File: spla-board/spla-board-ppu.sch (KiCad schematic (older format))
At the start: 20 parts, among them J15 J_DPULL, J5 J_PPURESET, U10 SNES_PPU1, U11 SNES_PPU2, U12 VRAM, U13 VRAM

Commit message: schematic: Add Digikey and ManufacturerId fields to big components.
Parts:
- U10, U11, U12, U13: Digikey (none) -> N/A; Manufacturer Id (none) -> N/A
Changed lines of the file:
@@
 F 2 "SPLA:QFP-100_14x20mm_P0.635mm" H 5700 8300 50  0001 C CNN
 F 3 "" H 5700 8300 50  0001 C CNN
+F 4 "N/A" H 5650 6100 50  0001 C CNN "Digikey"
+F 5 "N/A" H 5650 6100 50  0001 C CNN "Manufacturer Id"
 	1    5650 6100
 	1    0    0    -1
@@
 F 2 "SPLA:SOP-28_17x8mm_P1.27mm" H 9050 4050 50  0001 C CNN
 F 3 "" H 9050 4050 50  0001 C CNN
+F 4 "N/A" H 9050 4050 50  0001 C CNN "Digikey"
+F 5 "N/A" H 9050 4050 50  0001 C CNN "Manufacturer Id"
 	1    9050 4050
 	1    0    0    -1
@@
 F 2 "SPLA:SOP-28_17x8mm_P1.27mm" H 9050 6350 50  0001 C CNN
 F 3 "" H 9050 6350 50  0001 C CNN
+F 4 "N/A" H 9050 6350 50  0001 C CNN "Digikey"
+F 5 "N/A" H 9050 6350 50  0001 C CNN "Manufacturer Id"
 	1    9050 6350
 	1    0    0    -1
@@
 F 2 "SPLA:QFP-100_14x20mm_P0.635mm" H 12250 8300 50  0001 C CNN
 F 3 "" H 12250 8300 50  0001 C CNN
+F 4 "N/A" H 12200 6100 50  0001 C CNN "Digikey"
+F 5 "N/A" H 12200 6100 50  0001 C CNN "Manufacturer Id"
 	1    12200 6100
 	1    0    0    -1

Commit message: schematic: Add part numbers for pinheaders (albeit that these are breakaways, and it's not one-per-part).
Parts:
- J15, J5: Digikey (none) -> S1011EC-40-ND; Manufacturer Id (none) -> PRPC040SAAN-RC
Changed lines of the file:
@@
 F 2 "Connector_PinHeader_2.54mm:PinHeader_1x03_P2.54mm_Vertical" H 3250 9600 50  0001 C CNN
 F 3 "~" H 3250 9600 50  0001 C CNN
+F 4 "S1011EC-40-ND" H 3250 9600 50  0001 C CNN "Digikey"
+F 5 "PRPC040SAAN-RC" H 3250 9600 50  0001 C CNN "Manufacturer Id"
 	1    3250 9600
 	-1   0    0    1
@@
 F 2 "Connector_PinHeader_2.54mm:PinHeader_1x03_P2.54mm_Vertical" H 8050 1900 50  0001 C CNN
 F 3 "~" H 8050 1900 50  0001 C CNN
+F 4 "S1011EC-40-ND" H 8050 1900 50  0001 C CNN "Digikey"
+F 5 "PRPC040SAAN-RC" H 8050 1900 50  0001 C CNN "Manufacturer Id"
 	1    8050 1900
 	0    -1   -1   0

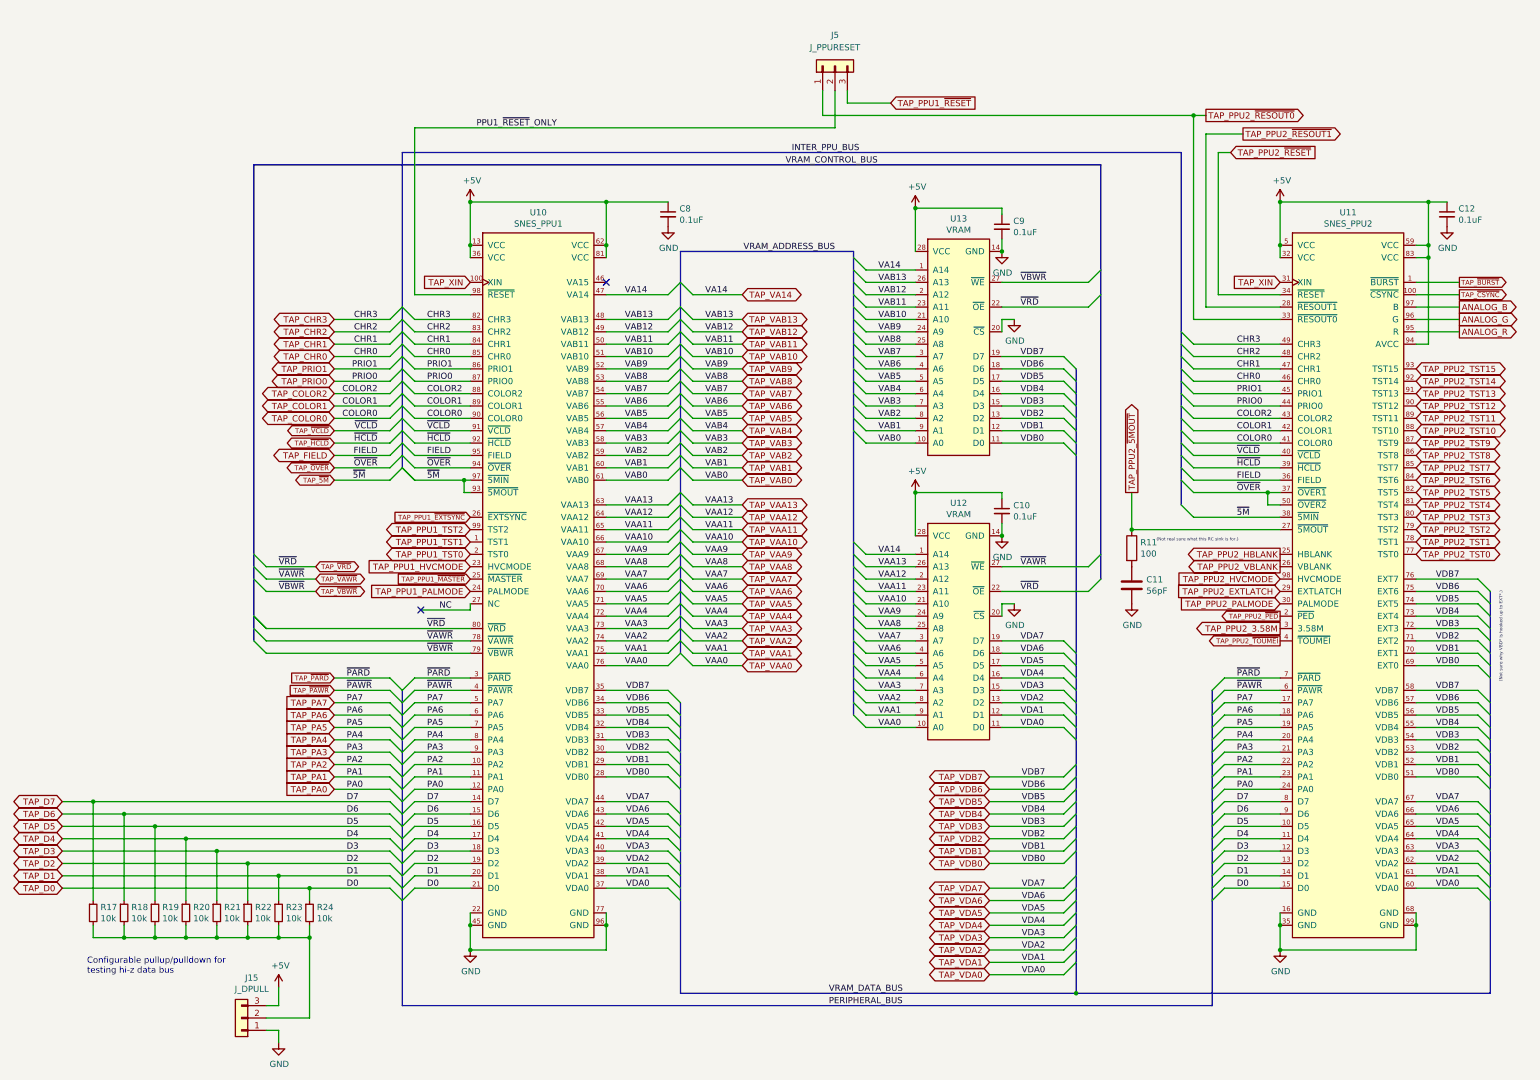
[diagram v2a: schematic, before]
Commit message: schematic/pcb: Add BoM-only symbols.
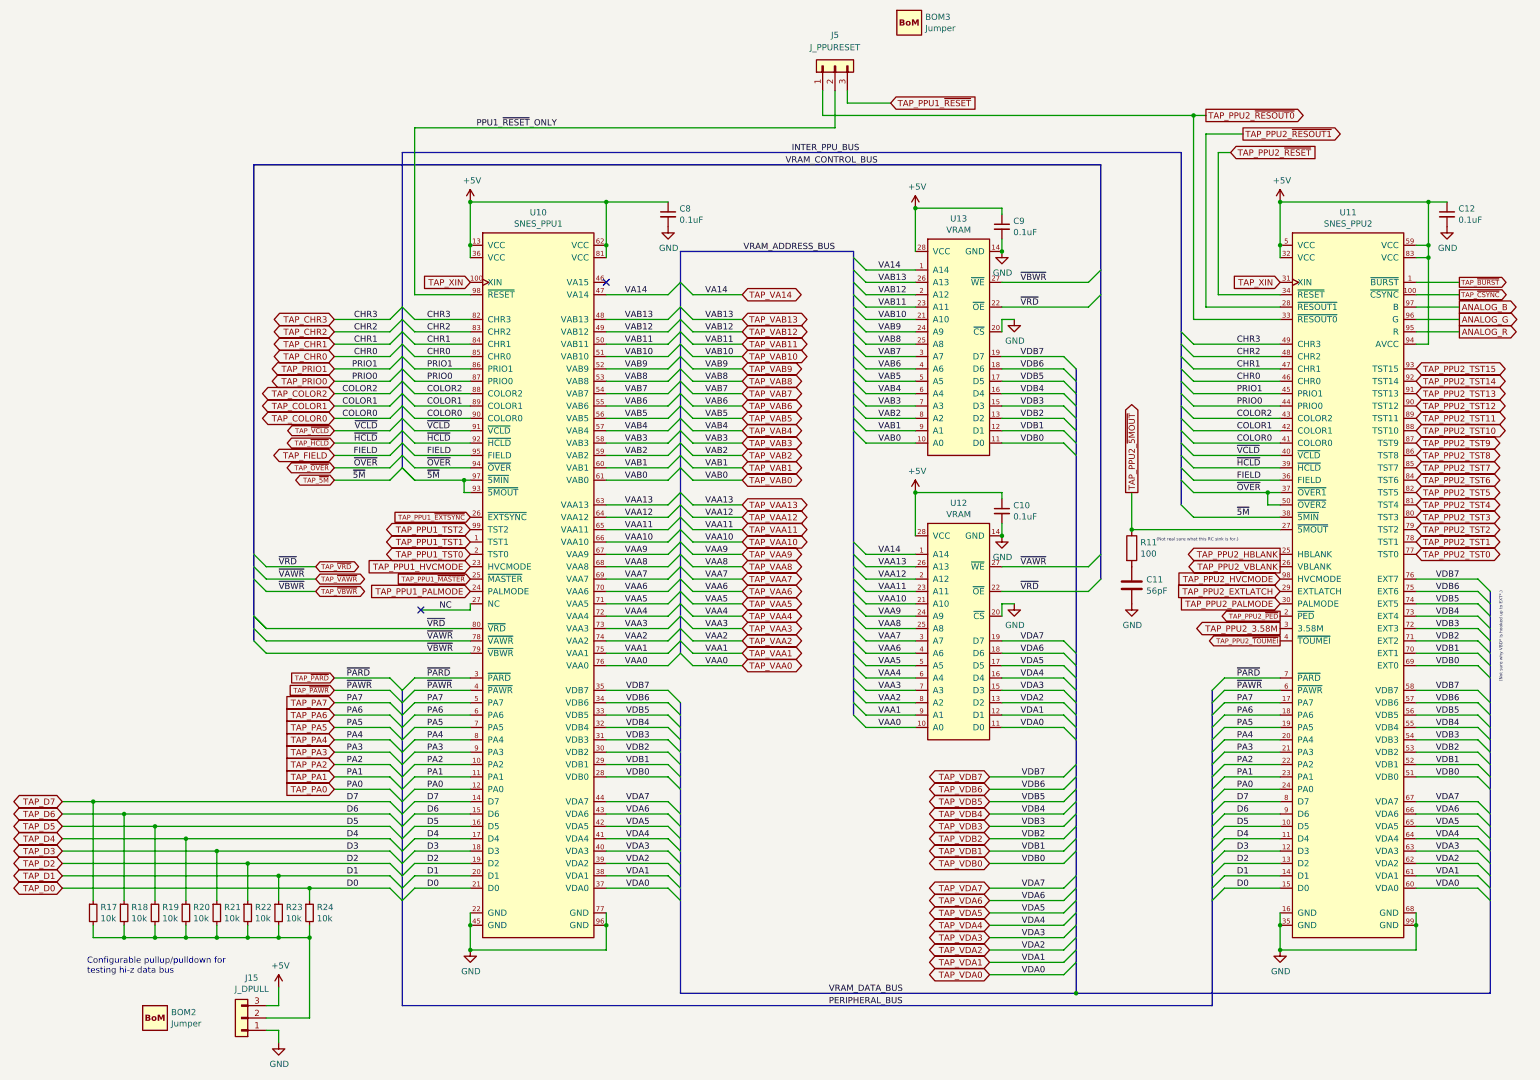
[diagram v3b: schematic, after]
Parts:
- added BOM2, BOM3: Jumper, SPLA:BoM, symbol SPLA:BomExtra
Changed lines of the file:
@@
 Wire Wire Line
 	4650 2400 8050 2400
+$Comp
+L SPLA:BomExtra BOM3
+U 1 1 5EAB9445
+P 8650 1550
+F 0 "BOM3" H 8780 1596 50  0000 L CNN
+F 1 "Jumper" H 8780 1505 50  0000 L CNN
+F 2 "SPLA:BoM" H 8650 1550 50  0001 C CNN
+F 3 "" H 8650 1550 50  0001 C CNN
+F 4 "S9337-ND" H 8650 1550 50  0001 C CNN "Digikey"
+F 5 "QPC02SXGN-RC" H 8650 1550 50  0001 C CNN "Manufacturer Id"
+	1    8650 1550
+	1    0    0    -1
+$EndComp
+$Comp
+L SPLA:BomExtra BOM2
+U 1 1 5EAB9764
+P 2550 9600
+F 0 "BOM2" H 2680 9646 50  0000 L CNN
+F 1 "Jumper" H 2680 9555 50  0000 L CNN
+F 2 "SPLA:BoM" H 2550 9600 50  0001 C CNN
+F 3 "" H 2550 9600 50  0001 C CNN
+F 4 "S9337-ND" H 2550 9600 50  0001 C CNN "Digikey"
+F 5 "QPC02SXGN-RC" H 2550 9600 50  0001 C CNN "Manufacturer Id"
+	1    2550 9600
+	1    0    0    -1
+$EndComp
 Wire Bus Line
 	10200 2700 10200 6050

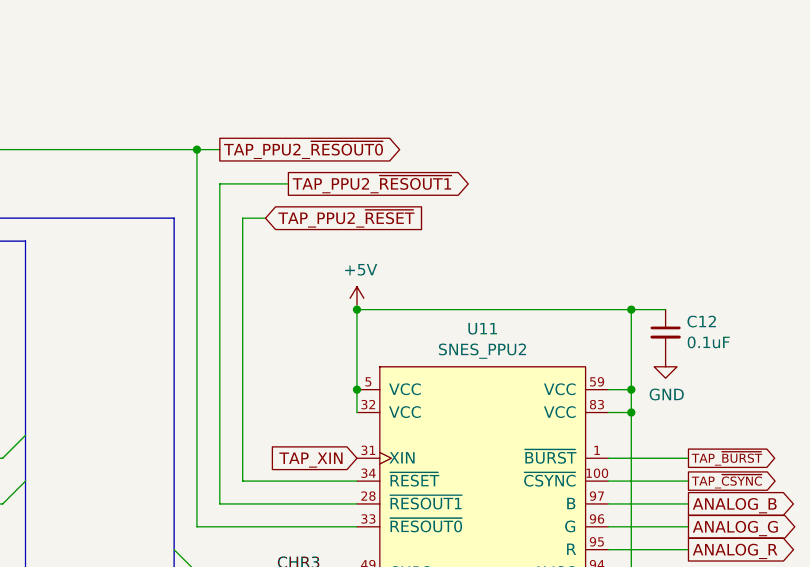
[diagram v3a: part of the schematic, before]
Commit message: schematic/pcb: Add pullup to SPI_CS and pulldown to PPU2_RESET.
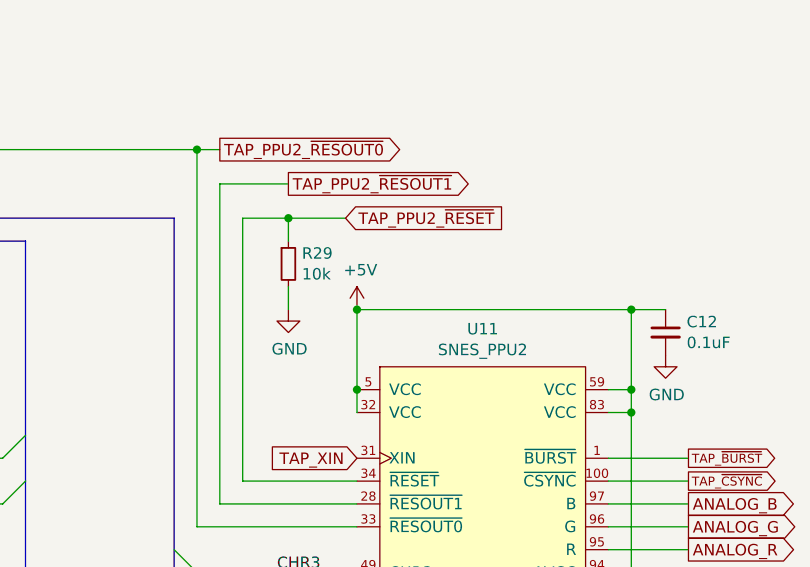
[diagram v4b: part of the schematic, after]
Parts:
- added R29: 10k, Resistor_SMD:R_0603_1608Metric, symbol Device:R_Small
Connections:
- net GND: now also R29.2
- net TAP_PPU2_~RESET~: now also R29.1
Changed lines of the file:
@@
 Connection ~ 12750 8850
 Wire Wire Line
-	11150 2600 11250 2600
+	11150 2600 11350 2600
 Connection ~ 10950 2300
 Wire Wire Line
@@
 Wire Wire Line
 	11150 2600 11150 3750
-Text GLabel 11250 2600 2    50   Input ~ 0
+Text GLabel 11600 2600 2    50   Input ~ 0
 TAP_PPU2_~RESET~
 Text GLabel 11050 2300 2    50   Output ~ 0
@@
 	1    0    0    -1
 $EndComp
+$Comp
+L Device:R_Small R29
+U 1 1 5EABD7FF
+P 11350 2800
+F 0 "R29" H 11409 2846 50  0000 L CNN
+F 1 "10k" H 11409 2755 50  0000 L CNN
+F 2 "Resistor_SMD:R_0603_1608Metric" H 11350 2800 50  0001 C CNN
+F 3 "~" H 11350 2800 50  0001 C CNN
+	1    11350 2800
+	1    0    0    -1
+$EndComp
+$Comp
+L power:GND #PWR0231
+U 1 1 5EABDF33
+P 11350 3000
+F 0 "#PWR0231" H 11350 2750 50  0001 C CNN
+F 1 "GND" H 11355 2827 50  0000 C CNN
+F 2 "" H 11350 3000 50  0001 C CNN
+F 3 "" H 11350 3000 50  0001 C CNN
+	1    11350 3000
+	1    0    0    -1
+$EndComp
+Wire Wire Line
+	11350 3000 11350 2900
+Wire Wire Line
+	11350 2700 11350 2600
 Wire Bus Line
 	10200 2700 10200 6050
@@
 Wire Bus Line
 	10000 4350 10000 9400
+Connection ~ 11350 2600
+Wire Wire Line
+	11350 2600 11600 2600
 $EndSCHEMATC

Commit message: bom: Add manufacturers.
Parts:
- BOM2, BOM3, J15, J5: Manufacturer (none) -> Sullins Connector Solutions
- U10: Manufacturer (none) -> Nintendo; Manufacturer Id N/A -> 5C77-01
- U11: Manufacturer (none) -> Nintendo; Manufacturer Id N/A -> 5C78-03
- U12, U13: Manufacturer (none) -> Mosel; Manufacturer Id N/A -> MS62256DL-10FC
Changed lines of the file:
@@
 F 3 "" H 5700 8300 50  0001 C CNN
 F 4 "N/A" H 5650 6100 50  0001 C CNN "Digikey"
-F 5 "N/A" H 5650 6100 50  0001 C CNN "Manufacturer Id"
+F 5 "5C77-01" H 5650 6100 50  0001 C CNN "Manufacturer Id"
+F 6 "Nintendo" H 5650 6100 50  0001 C CNN "Manufacturer"
 	1    5650 6100
 	1    0    0    -1
@@
 F 3 "" H 9050 4050 50  0001 C CNN
 F 4 "N/A" H 9050 4050 50  0001 C CNN "Digikey"
-F 5 "N/A" H 9050 4050 50  0001 C CNN "Manufacturer Id"
+F 5 "MS62256DL-10FC" H 9050 4050 50  0001 C CNN "Manufacturer Id"
+F 6 "Mosel" H 9050 4050 50  0001 C CNN "Manufacturer"
 	1    9050 4050
 	1    0    0    -1
@@
 F 3 "" H 9050 6350 50  0001 C CNN
 F 4 "N/A" H 9050 6350 50  0001 C CNN "Digikey"
-F 5 "N/A" H 9050 6350 50  0001 C CNN "Manufacturer Id"
+F 5 "MS62256DL-10FC" H 9050 6350 50  0001 C CNN "Manufacturer Id"
+F 6 "Mosel" H 9050 6350 50  0001 C CNN "Manufacturer"
 	1    9050 6350
 	1    0    0    -1
@@
 F 4 "S1011EC-40-ND" H 3250 9600 50  0001 C CNN "Digikey"
 F 5 "PRPC040SAAN-RC" H 3250 9600 50  0001 C CNN "Manufacturer Id"
+F 6 "Sullins Connector Solutions" H 3250 9600 50  0001 C CNN "Manufacturer"
 	1    3250 9600
 	-1   0    0    1
@@
 F 3 "" H 12250 8300 50  0001 C CNN
 F 4 "N/A" H 12200 6100 50  0001 C CNN "Digikey"
-F 5 "N/A" H 12200 6100 50  0001 C CNN "Manufacturer Id"
+F 5 "5C78-03" H 12200 6100 50  0001 C CNN "Manufacturer Id"
+F 6 "Nintendo" H 12200 6100 50  0001 C CNN "Manufacturer"
 	1    12200 6100
 	1    0    0    -1
@@
 F 4 "S1011EC-40-ND" H 8050 1900 50  0001 C CNN "Digikey"
 F 5 "PRPC040SAAN-RC" H 8050 1900 50  0001 C CNN "Manufacturer Id"
+F 6 "Sullins Connector Solutions" H 8050 1900 50  0001 C CNN "Manufacturer"
 	1    8050 1900
 	0    -1   -1   0
@@
 F 4 "S9337-ND" H 8650 1550 50  0001 C CNN "Digikey"
 F 5 "QPC02SXGN-RC" H 8650 1550 50  0001 C CNN "Manufacturer Id"
+F 6 "Sullins Connector Solutions" H 8650 1550 50  0001 C CNN "Manufacturer"
 	1    8650 1550
 	1    0    0    -1
@@
 F 4 "S9337-ND" H 2550 9600 50  0001 C CNN "Digikey"
 F 5 "QPC02SXGN-RC" H 2550 9600 50  0001 C CNN "Manufacturer Id"
+F 6 "Sullins Connector Solutions" H 2550 9600 50  0001 C CNN "Manufacturer"
 	1    2550 9600
 	1    0    0    -1

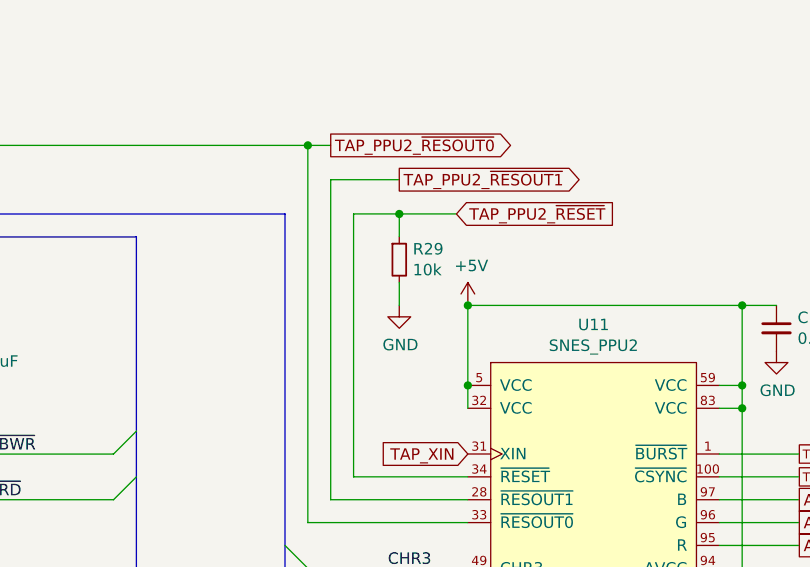
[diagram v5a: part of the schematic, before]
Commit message: schematic/pcb: Move PPU RESET pulldowns before level shifter.
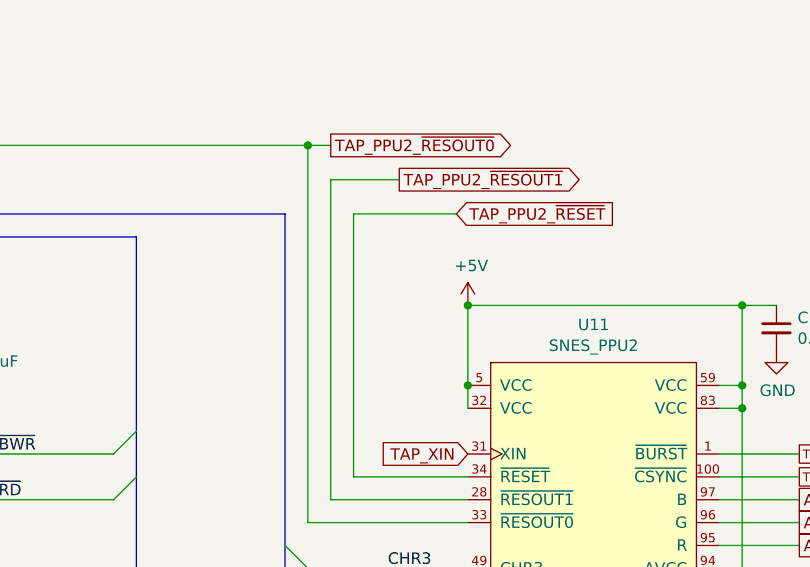
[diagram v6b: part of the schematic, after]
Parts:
- removed R29: 10k, Resistor_SMD:R_0603_1608Metric, symbol Device:R_Small
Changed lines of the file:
@@
 	12750 8750 12750 8850
 Connection ~ 12750 8850
-Wire Wire Line
-	11150 2600 11350 2600
 Connection ~ 10950 2300
 Wire Wire Line
@@
 Wire Wire Line
 	11150 2600 11150 3750
-Text GLabel 11600 2600 2    50   Input ~ 0
-TAP_PPU2_~RESET~
 Text GLabel 11050 2300 2    50   Output ~ 0
 TAP_PPU2_~RESOUT0~
@@
 	1    0    0    -1
 $EndComp
-$Comp
-L Device:R_Small R29
-U 1 1 5EABD7FF
-P 11350 2800
-F 0 "R29" H 11409 2846 50  0000 L CNN
-F 1 "10k" H 11409 2755 50  0000 L CNN
-F 2 "Resistor_SMD:R_0603_1608Metric" H 11350 2800 50  0001 C CNN
-F 3 "~" H 11350 2800 50  0001 C CNN
-	1    11350 2800
-	1    0    0    -1
-$EndComp
-$Comp
-L power:GND #PWR0231
-U 1 1 5EABDF33
-P 11350 3000
-F 0 "#PWR0231" H 11350 2750 50  0001 C CNN
-F 1 "GND" H 11355 2827 50  0000 C CNN
-F 2 "" H 11350 3000 50  0001 C CNN
-F 3 "" H 11350 3000 50  0001 C CNN
-	1    11350 3000
-	1    0    0    -1
-$EndComp
-Wire Wire Line
-	11350 3000 11350 2900
-Wire Wire Line
-	11350 2700 11350 2600
 Wire Bus Line
 	10200 2700 10200 6050
@@
 	3350 2700 3350 6550
 Wire Bus Line
-	4550 2600 4550 5150
+	6800 7050 6800 9400
 Wire Bus Line
-	10850 2600 10850 5450
+	13350 6150 13350 9400
 Wire Bus Line
-	6800 7050 6800 9400
+	10000 4350 10000 9400
 Wire Bus Line
 	11100 6950 11100 9500
@@
 	4550 6950 4550 9500
 Wire Bus Line
-	6800 3400 6800 6650
+	10850 2600 10850 5450
 Wire Bus Line
 	8200 3400 8200 7150
 Wire Bus Line
-	13350 6150 13350 9400
+	6800 3400 6800 6650
 Wire Bus Line
-	10000 4350 10000 9400
-Connection ~ 11350 2600
+	4550 2600 4550 5150
 Wire Wire Line
-	11350 2600 11600 2600
+	11150 2600 11600 2600
+Text GLabel 11600 2600 2    50   Input ~ 0
+TAP_PPU2_~RESET~
 $EndSCHEMATC
